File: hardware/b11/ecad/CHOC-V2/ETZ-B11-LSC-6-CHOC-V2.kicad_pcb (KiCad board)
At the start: 2 copper layers, 131.5 x 85.8 mm, 44 parts, among them SW1 Kailh_socket_PG1350, SW10 Kailh_socket_PG1350, SW11 Kailh_socket_PG1350, SW12 Kailh_socket_PG1350, SW13 Kailh_socket_PG1350, SW14 Kailh_socket_PG1350, SW15 Kailh_socket_PG1350, SW16 Kailh_socket_PG1350, SW17 Kailh_socket_PG1350, SW18 Kailh_socket_PG1350, SW19 Kailh_socket_PG1350, SW2 Kailh_socket_PG1350, SW20 Kailh_socket_PG1350, SW21 Kailh_socket_PG1350, SW22 Kailh_socket_PG1350, SW3 Kailh_socket_PG1350, SW4 Kailh_socket_PG1350, SW5 Kailh_socket_PG1350, SW6 Kailh_socket_PG1350, SW7 Kailh_socket_PG1350, SW8 Kailh_socket_PG1350, SW9 Kailh_socket_PG1350

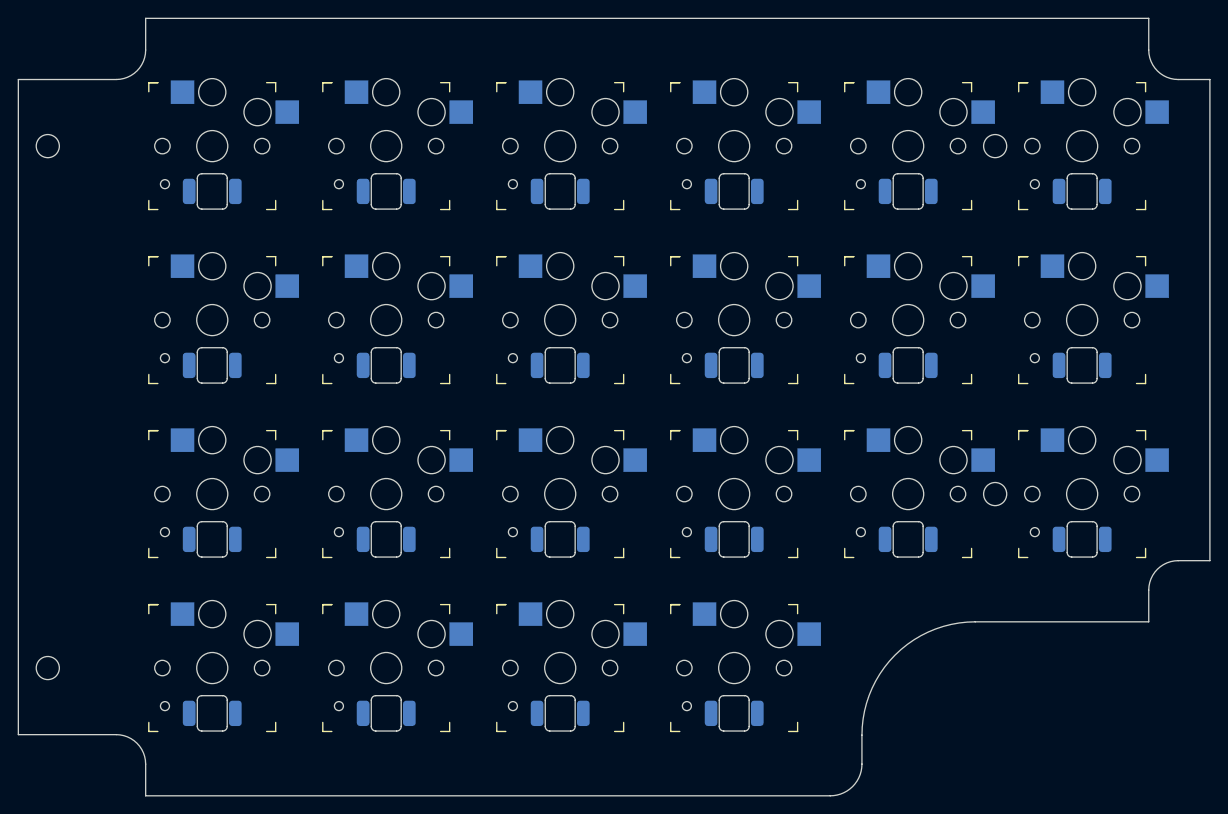
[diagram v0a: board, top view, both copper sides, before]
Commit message: refactor(hardware/b11): restructure ecad + tools, add KS-33 boards
- Rename PCB files: *-N → *-MX, *-L → *-CHOC-V2
- Reorganise ecad/ into per-family subfolders (MX/, CHOC-V2/, KS-33/)
- Add 8 blank KS-33 boards (outline only, human-populated ad-hoc)
- Apply JLCPCB-validated stackup (white/black/FR4 natural/black/white)
  to all 24 boards; SP boards at correct family thickness
- Add hardware/b11/tools/: config.py, placement.py, place-switch-sockets.py,
  place-switch-leds.py, place-display-leds.py — family-aware, non-destructive
- Archive old placement + generation scripts to hardware/scripts/_archive/
- Remove switch-origins.yaml (replaced by GRID_ORIGINS in config.py)
- Add PLAN.md tracking refactor progress

Co-Authored-By: Claude Sonnet 4.6 <noreply@anthropic.com>
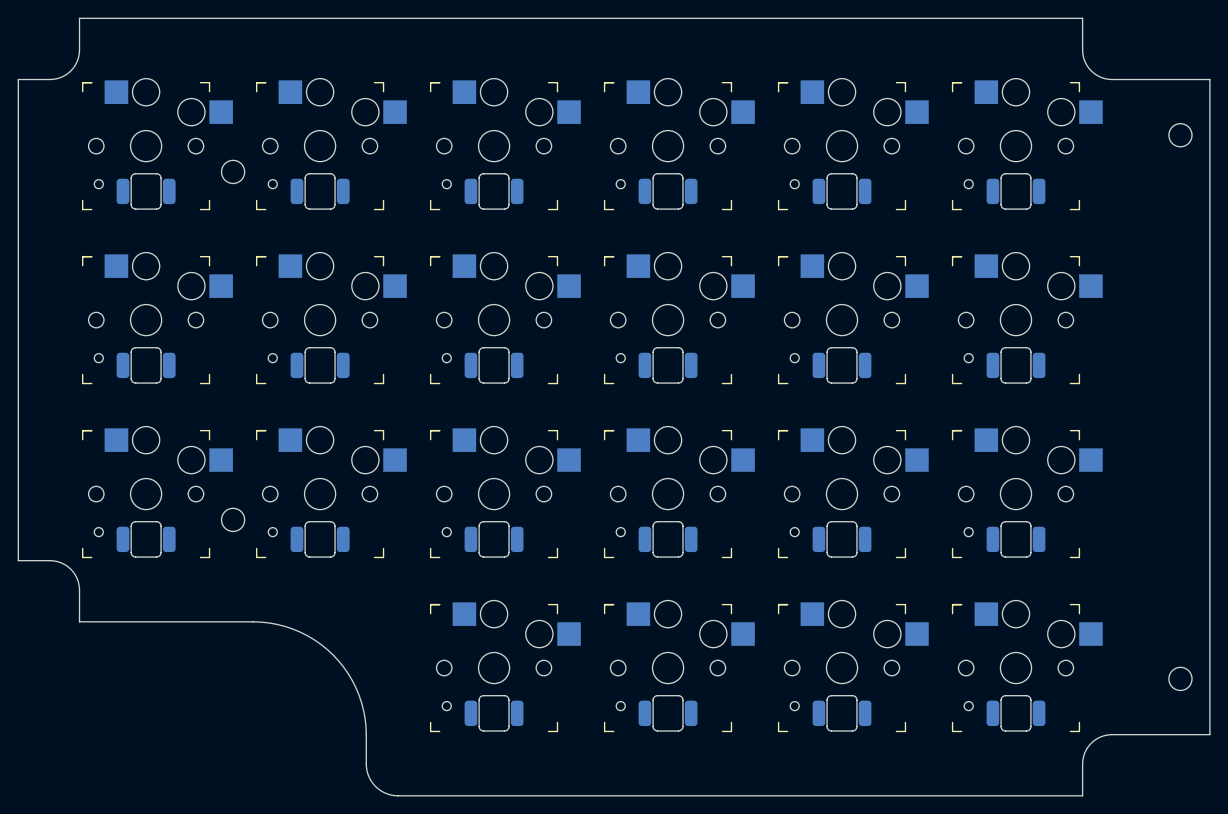
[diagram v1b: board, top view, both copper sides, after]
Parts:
- moved LED1 103.3 mm to (96.8, 78.3)
- moved LED13 103.3 mm to (96.8, 116.7)
- moved LED7 103.3 mm to (96.8, 97.5)
- moved SW1 103.3 mm to (96.8, 73.3)
- moved SW13 103.3 mm to (96.8, 111.7)
- moved SW7 103.3 mm to (96.8, 92.5)
- moved LED12 88.7 mm to (192.8, 97.5)
- moved LED18 88.7 mm to (192.8, 116.7)
- moved LED22 88.7 mm to (192.8, 135.9)
- moved LED6 88.7 mm to (192.8, 78.3)
- moved SW12 88.7 mm to (192.8, 92.5)
- moved SW18 88.7 mm to (192.8, 111.7)
- moved SW22 88.7 mm to (192.8, 130.9)
- moved SW6 88.7 mm to (192.8, 73.3)
- moved LED14 64.9 mm to (116.0, 116.7)
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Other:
- outline, holes or cut-outs redrawn
